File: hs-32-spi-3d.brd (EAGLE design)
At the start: 15.2 x 23.5 mm, 25 parts, among them U1 RHD2132_QFN, U2 BNO055, U3 TLV70725

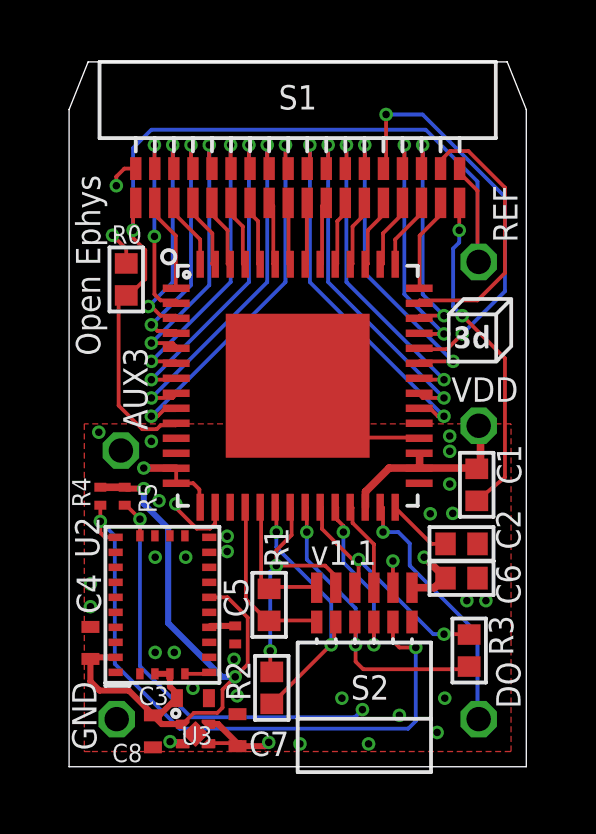
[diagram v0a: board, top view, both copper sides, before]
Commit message: Added EEPROM.
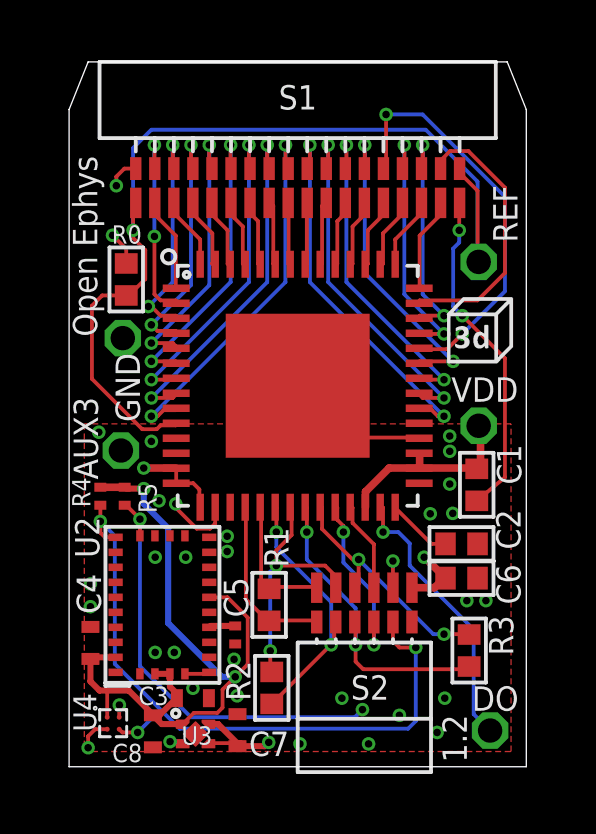
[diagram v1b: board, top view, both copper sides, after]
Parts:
- added U4: 24CW640T-I/CS0668, 24CW640T-I_CS0668:4-BALL_WAFFER_0.4MMX0.4MM
- moved GND 12.7 mm to (1.79, 14.3)
- moved DO 0.54 mm to (14.0, 1.21)
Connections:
- net +2V5: now also U4.A1
- net BNO_SCL: now also U4.B1
- net BNO_SDA: now also U4.B2
- net GND: now also U4.A2
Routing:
- net BNO_SCL: track 21.2 -> 31.9 mm, vias 3 -> 4
- net BNO_SDA: track 21.4 -> 23.1 mm, vias 2 -> 3
- net N$1: track 31.2 -> 32.3 mm
- net +2V5: track 23.5 -> 24.4 mm
- net N$43: track 8.76 -> 9.30 mm
- net GND: track 19.0 -> 19.4 mm, vias 32 -> 33
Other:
- board text added: "1.2"
- board text removed: "v1.1"
